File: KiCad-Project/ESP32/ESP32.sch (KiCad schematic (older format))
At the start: 14 parts, among them J3 UART, SW1 RESET, U3 AMS1117-3.3, U4 ESP32-WROOM-32

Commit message: swap out 603 resistors for 805
Give us more room to work with if we have to fix something.
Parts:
- R10: footprint Resistor_SMD:R_0201_0603Metric -> Resistor_SMD:R_0805_2012Metric; JLCPCB_PNUM C8218 -> C17540; MFG_PNUM 0603WAF2000T5E -> 0805W8F2000T5E; PACKAGE 0603 -> 0805
- R8: footprint Resistor_SMD:R_0201_0603Metric -> Resistor_SMD:R_0805_2012Metric; JLCPCB_PNUM C21190 -> C17513; MFG_PNUM 0603WAF1001T5E -> 0805W8F1001T5E; PACKAGE 0603 -> 0805
- R9: footprint Resistor_SMD:R_0201_0603Metric -> Resistor_SMD:R_0805_2012Metric; JLCPCB_PNUM C25804 -> C17414; MFG_PNUM 0603WAF1002T5E -> 0805W8F1002T5E; PACKAGE 0603 -> 0805
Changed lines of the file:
@@
 F 0 "R8" H 1609 1796 50  0000 L CNN
 F 1 "1K" H 1609 1705 50  0000 L CNN
-F 2 "Resistor_SMD:R_0201_0603Metric" H 1550 1750 50  0001 C CNN
+F 2 "Resistor_SMD:R_0805_2012Metric" H 1550 1750 50  0001 C CNN
 F 3 "~" H 1550 1750 50  0001 C CNN
-F 4 "C21190" H 1550 1750 50  0001 C CNN "JLCPCB_PNUM"
-F 5 "0603WAF1001T5E" H 1550 1750 50  0001 C CNN "MFG_PNUM"
-F 6 "0603" H 1550 1750 50  0001 C CNN "PACKAGE"
+F 4 "C17513" H 1550 1750 50  0001 C CNN "JLCPCB_PNUM"
+F 5 "0805W8F1001T5E" H 1550 1750 50  0001 C CNN "MFG_PNUM"
+F 6 "0805" H 1550 1750 50  0001 C CNN "PACKAGE"
 F 7 "JLCPCB" H 1550 1750 50  0001 C CNN "SUPPLIER"
 	1    1550 1750
@@
 F 0 "R9" H 2359 3596 50  0000 L CNN
 F 1 "10K" H 2359 3505 50  0000 L CNN
-F 2 "Resistor_SMD:R_0201_0603Metric" H 2300 3550 50  0001 C CNN
+F 2 "Resistor_SMD:R_0805_2012Metric" H 2300 3550 50  0001 C CNN
 F 3 "~" H 2300 3550 50  0001 C CNN
-F 4 "C25804" H 2300 3550 50  0001 C CNN "JLCPCB_PNUM"
-F 5 "0603WAF1002T5E" H 2300 3550 50  0001 C CNN "MFG_PNUM"
-F 6 "0603" H 2300 3550 50  0001 C CNN "PACKAGE"
+F 4 "C17414" H 2300 3550 50  0001 C CNN "JLCPCB_PNUM"
+F 5 "0805W8F1002T5E" H 2300 3550 50  0001 C CNN "MFG_PNUM"
+F 6 "0805" H 2300 3550 50  0001 C CNN "PACKAGE"
 F 7 "JLCPCB" H 2300 3550 50  0001 C CNN "SUPPLIER"
 	1    2300 3550
@@
 F 0 "R10" V 9050 2500 50  0000 L CNN
 F 1 "200" V 9250 2500 50  0000 L CNN
-F 2 "Resistor_SMD:R_0201_0603Metric" H 9150 2550 50  0001 C CNN
+F 2 "Resistor_SMD:R_0805_2012Metric" H 9150 2550 50  0001 C CNN
 F 3 "~" H 9150 2550 50  0001 C CNN
-F 4 "C8218" H 9150 2550 50  0001 C CNN "JLCPCB_PNUM"
-F 5 "0603WAF2000T5E" H 9150 2550 50  0001 C CNN "MFG_PNUM"
-F 6 "0603" H 9150 2550 50  0001 C CNN "PACKAGE"
+F 4 "C17540" H 9150 2550 50  0001 C CNN "JLCPCB_PNUM"
+F 5 "0805W8F2000T5E" H 9150 2550 50  0001 C CNN "MFG_PNUM"
+F 6 "0805" H 9150 2550 50  0001 C CNN "PACKAGE"
 F 7 "JLCPCB" H 9150 2550 50  0001 C CNN "SUPPLIER"
 	1    9150 2550

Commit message: Fixes in prep for printing
Making sure tolerance are in-spec for JLC PCB
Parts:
- U4: JLCPCB_PNUM (none) -> C82899; MFG_PNUM (none) -> ESP32-WROOM-32; PACKAGE (none) -> QFN-38_EP_18.0x25.0x1.27P; SUPPLIER (none) -> JLCPCB
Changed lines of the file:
@@
 F 2 "RF_Module:ESP32-WROOM-32" H 7750 1550 50  0001 C CNN
 F 3 "https://www.espressif.com/sites/default/files/documentation/esp32-wroom-32_datasheet_en.pdf" H 7450 3100 50  0001 C CNN
+F 4 "C82899" H 7750 3050 50  0001 C CNN "JLCPCB_PNUM"
+F 5 "ESP32-WROOM-32" H 7750 3050 50  0001 C CNN "MFG_PNUM"
+F 6 "QFN-38_EP_18.0x25.0x1.27P" H 7750 3050 50  0001 C CNN "PACKAGE"
+F 7 "JLCPCB" H 7750 3050 50  0001 C CNN "SUPPLIER"
 	1    7750 3050
 	1    0    0    -1

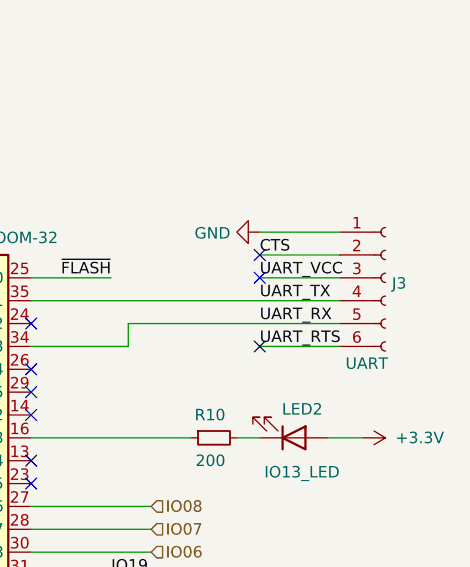
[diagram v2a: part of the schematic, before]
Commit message: Fix pin header
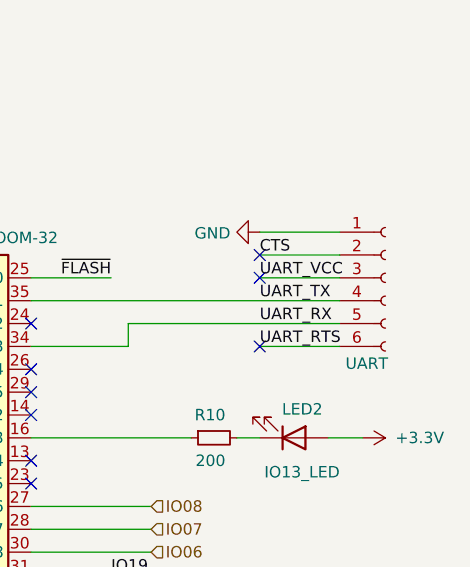
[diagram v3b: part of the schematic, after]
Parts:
- J3: footprint Connector_PinHeader_1.27mm:PinHeader_1x06_P1.27mm_Vertical -> Connector_PinSocket_2.54mm:PinSocket_1x06_P2.54mm_Vertical
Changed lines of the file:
@@
 U 1 1 61877E1E
 P 9900 1850
-F 0 "J3" H 9928 1826 50  0000 L CNN
+F 0 "J3" H 9928 1826 50  0001 L CNN
 F 1 "UART" H 9725 1475 50  0000 L CNN
-F 2 "Connector_PinHeader_1.27mm:PinHeader_1x06_P1.27mm_Vertical" H 9900 1850 50  0001 C CNN
+F 2 "Connector_PinSocket_2.54mm:PinSocket_1x06_P2.54mm_Vertical" H 9900 1850 50  0001 C CNN
 F 3 "~" H 9900 1850 50  0001 C CNN
 F 4 "Mouser" H 9900 1850 50  0001 C CNN "SUPPLIER"

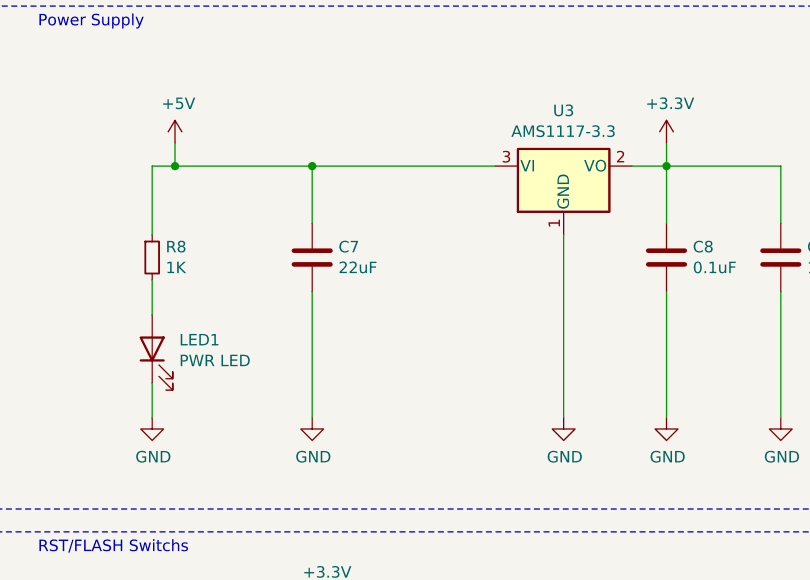
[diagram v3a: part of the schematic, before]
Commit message: Removed reverse voltage and increased size of power traces
Reverse voltage needed different components for 24 volt, and was a nice to have, so to keep cost down, opted to remove it.
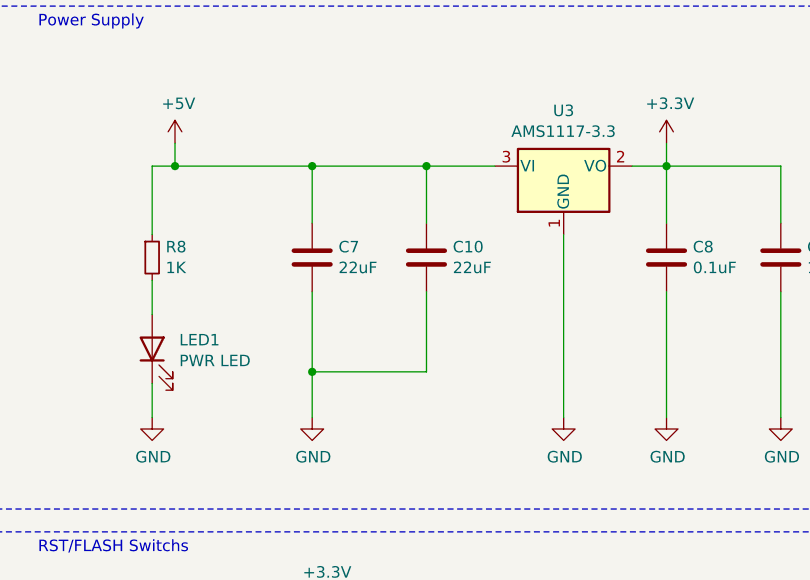
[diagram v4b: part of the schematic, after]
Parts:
- added C10: 22uF, Capacitor_SMD:C_0805_2012Metric, symbol Device:C
- JP1: footprint Connector_PinHeader_1.27mm:PinHeader_1x02_P1.27mm_Vertical -> Connector_PinHeader_2.54mm:PinHeader_1x02_P2.54mm_Vertical
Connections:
- net +5V: now also C10.1
- net GND: now also C10.2
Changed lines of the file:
@@
 $EndComp
 Wire Wire Line
-	3050 1350 2250 1350
+	3050 1350 2750 1350
 Wire Wire Line
 	1550 1350 1550 1650
@@
 $EndComp
 Wire Wire Line
-	2250 1900 2250 2450
+	2250 1900 2250 2250
 $Comp
 L power:GND #PWR018
@@
 Wire Wire Line
 	3100 4100 3100 3950
-Wire Wire Line
-	3100 3950 3450 3950
 Text Label 2850 3850 2    50   ~ 0
 ~RESET
@@
 UART_VCC
 NoConn ~ 9350 1850
-$Comp
-L Device:Jumper_NO_Small JP1
-U 1 1 6189F27D
-P 3550 3950
-F 0 "JP1" H 3550 4135 50  0000 C CNN
-F 1 "FLASH" H 3550 4044 50  0000 C CNN
-F 2 "Connector_PinHeader_1.27mm:PinHeader_1x02_P1.27mm_Vertical" H 3550 3950 50  0001 C CNN
-F 3 "~" H 3550 3950 50  0001 C CNN
-F 4 "Mouser" H 3550 3950 50  0001 C CNN "SUPPLIER"
-	1    3550 3950
-	1    0    0    -1
-$EndComp
-Wire Wire Line
-	3650 3950 4700 3950
 Wire Wire Line
 	8775 2050 8775 2150
@@
 Wire Wire Line
 	8350 2550 9050 2550
+Wire Wire Line
+	3650 3950 4700 3950
+Wire Wire Line
+	3100 3950 3450 3950
+$Comp
+L Device:Jumper_NO_Small JP1
+U 1 1 6189F27D
+P 3550 3950
+F 0 "JP1" H 3550 4135 50  0000 C CNN
+F 1 "FLASH" H 3550 4044 50  0000 C CNN
+F 2 "Connector_PinHeader_2.54mm:PinHeader_1x02_P2.54mm_Vertical" H 3550 3950 50  0001 C CNN
+F 3 "~" H 3550 3950 50  0001 C CNN
+F 4 "Mouser" H 3550 3950 50  0001 C CNN "SUPPLIER"
+	1    3550 3950
+	1    0    0    -1
+$EndComp
+$Comp
+L Device:C C10
+U 1 1 61B24BD4
+P 2750 1750
+F 0 "C10" H 2865 1796 50  0000 L CNN
+F 1 "22uF" H 2865 1705 50  0000 L CNN
+F 2 "Capacitor_SMD:C_0805_2012Metric" H 2788 1600 50  0001 C CNN
+F 3 "~" H 2750 1750 50  0001 C CNN
+F 4 "C45783" H 2750 1750 50  0001 C CNN "JLCPCB_PNUM"
+F 5 "CL21A226MAQNNNE" H 2750 1750 50  0001 C CNN "MFG_PNUM"
+F 6 "0805" H 2750 1750 50  0001 C CNN "PACKAGE"
+F 7 "JLCPCB" H 2750 1750 50  0001 C CNN "SUPPLIER"
+	1    2750 1750
+	1    0    0    -1
+$EndComp
+Wire Wire Line
+	2750 1600 2750 1350
+Connection ~ 2750 1350
+Wire Wire Line
+	2750 1350 2250 1350
+Wire Wire Line
+	2750 1900 2750 2250
+Wire Wire Line
+	2750 2250 2250 2250
+Connection ~ 2250 2250
+Wire Wire Line
+	2250 2250 2250 2450
 $EndSCHEMATC

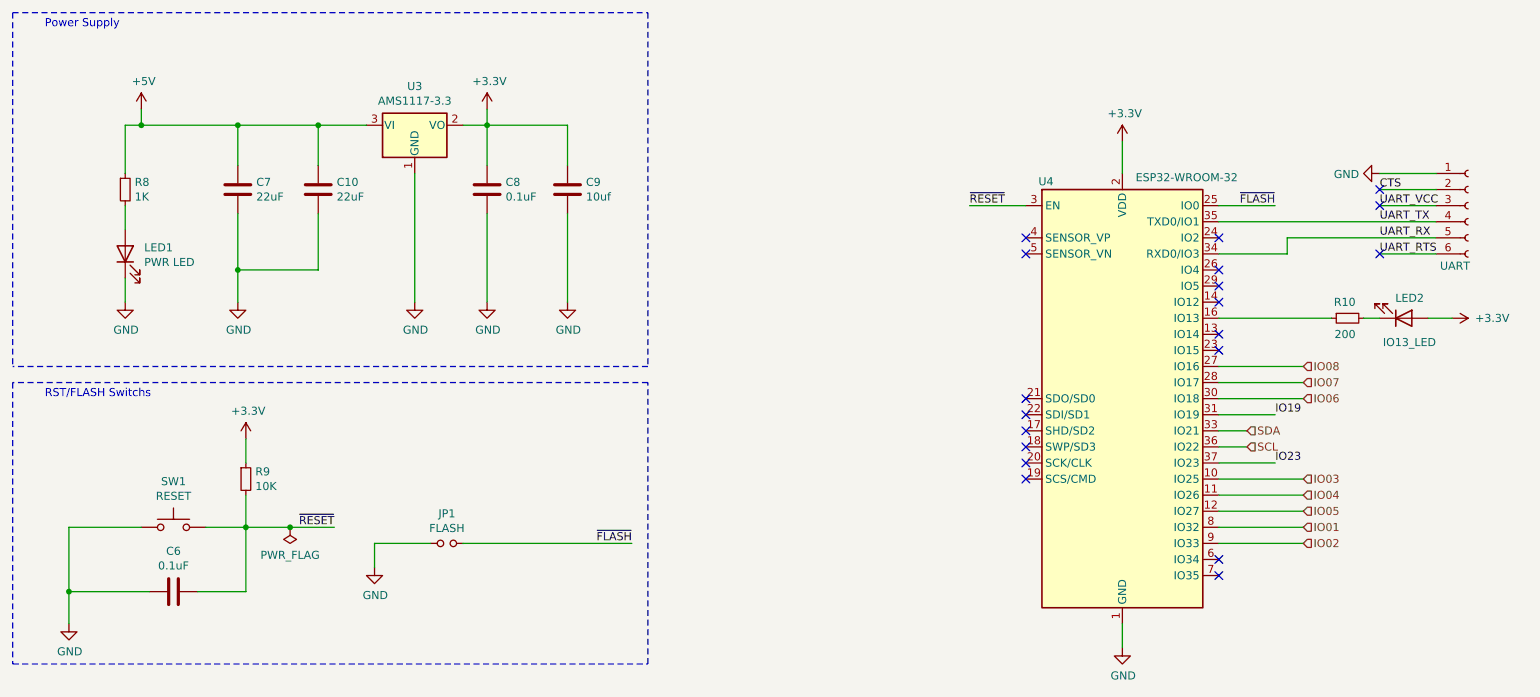
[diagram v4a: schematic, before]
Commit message: Jumper to connect UART VCC to 5v
Allow powering the 3v-5v side from the UART conector.
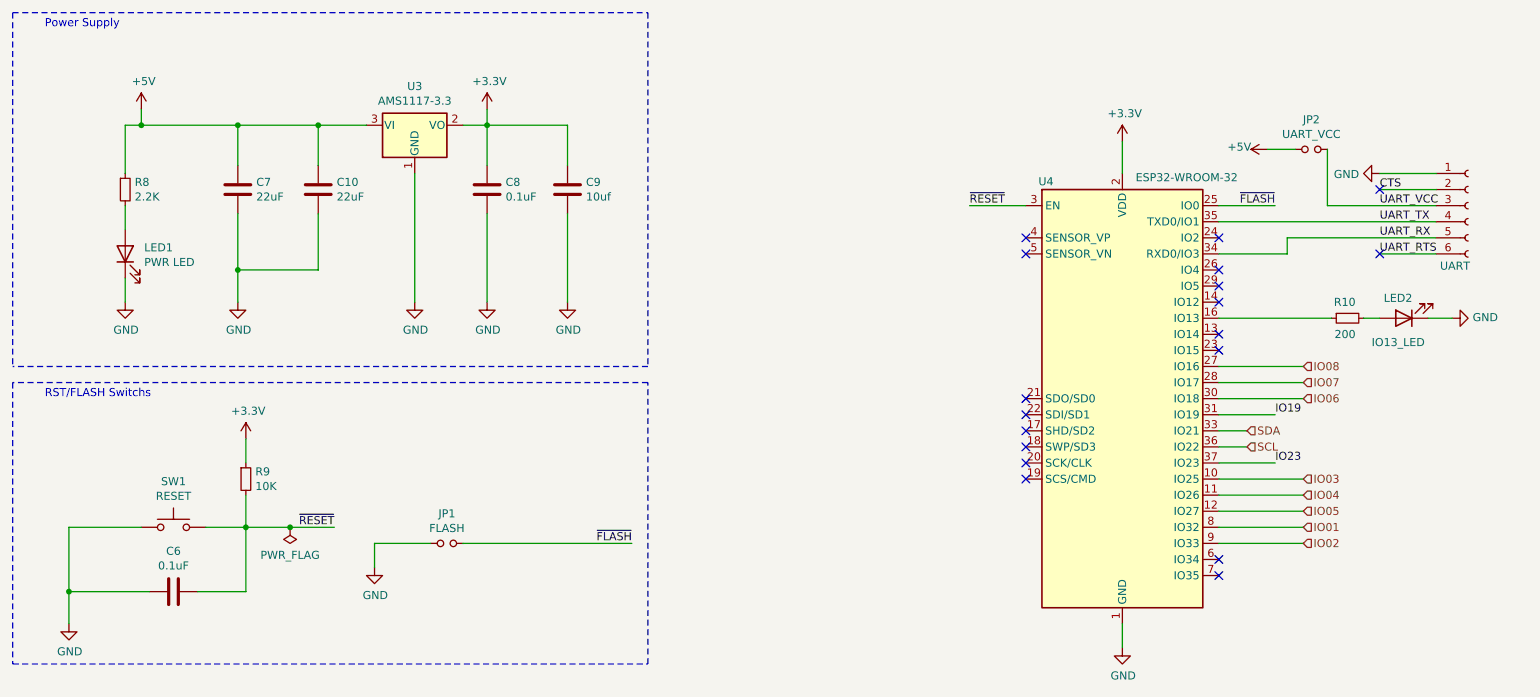
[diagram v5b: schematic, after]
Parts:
- added JP2: UART_VCC, Connector_PinHeader_2.54mm:PinHeader_1x02_P2.54mm_Vertical, symbol Device:Jumper_NO_Small
- R8: value 1K -> 2.2K; JLCPCB_PNUM C17513 -> C17520; MFG_PNUM 0805W8F1001T5E -> 0805W8F2201T5E
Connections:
- net +3V3: no longer LED2.2 (A)
- net +5V: now also JP2.1
- net GND: now also LED2.1 (K)
- net UART_VCC: now also JP2.2
- net at R10.2: now also LED2.2 (A); no longer LED2.1 (K)
- no-connect marks 19 -> 18
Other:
- moved on the sheet: LED2
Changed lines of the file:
@@
 P 1550 1750
 F 0 "R8" H 1609 1796 50  0000 L CNN
-F 1 "1K" H 1609 1705 50  0000 L CNN
+F 1 "2.2K" H 1609 1705 50  0000 L CNN
 F 2 "Resistor_SMD:R_0805_2012Metric" H 1550 1750 50  0001 C CNN
 F 3 "~" H 1550 1750 50  0001 C CNN
-F 4 "C17513" H 1550 1750 50  0001 C CNN "JLCPCB_PNUM"
-F 5 "0805W8F1001T5E" H 1550 1750 50  0001 C CNN "MFG_PNUM"
+F 4 "C17520" H 1550 1750 50  0001 C CNN "JLCPCB_PNUM"
+F 5 "0805W8F2201T5E" H 1550 1750 50  0001 C CNN "MFG_PNUM"
 F 6 "0805" H 1550 1750 50  0001 C CNN "PACKAGE"
 F 7 "JLCPCB" H 1550 1750 50  0001 C CNN "SUPPLIER"
@@
 	9700 2150 9350 2150
 Wire Wire Line
-	9700 1850 9350 1850
-Wire Wire Line
 	9700 1750 9350 1750
 Wire Wire Line
@@
 F 7 "JLCPCB" H 9500 2550 50  0001 C CNN "SUPPLIER"
 	1    9500 2550
-	1    0    0    1
+	-1   0    0    1
 $EndComp
 $Comp
@@
 Wire Wire Line
 	9350 2550 9250 2550
-$Comp
-L power:+3.3V #PWR022
-U 1 1 618A9CE7
-P 9800 2550
-F 0 "#PWR022" H 9800 2400 50  0001 C CNN
-F 1 "+3.3V" V 9800 2800 50  0000 C CNN
-F 2 "" H 9800 2550 50  0001 C CNN
-F 3 "" H 9800 2550 50  0001 C CNN
-	1    9800 2550
-	0    1    -1   0
-$EndComp
 Wire Wire Line
 	9800 2550 9650 2550
@@
 Text Label 9350 1850 0    50   ~ 0
 UART_VCC
-NoConn ~ 9350 1850
 Wire Wire Line
 	8775 2050 8775 2150
@@
 Wire Wire Line
 	2250 2250 2250 2450
+$Comp
+L power:+5V #PWR023
+U 1 1 61B4BBED
+P 8650 1500
+F 0 "#PWR023" H 8650 1350 50  0001 C CNN
+F 1 "+5V" V 8665 1673 50  0000 C CNN
+F 2 "" H 8650 1500 50  0001 C CNN
+F 3 "" H 8650 1500 50  0001 C CNN
+	1    8650 1500
+	0    -1   -1   0
+$EndComp
+$Comp
+L Device:Jumper_NO_Small JP2
+U 1 1 61B4F51D
+P 8925 1500
+F 0 "JP2" H 8925 1685 50  0000 C CNN
+F 1 "UART_VCC" H 8925 1594 50  0000 C CNN
+F 2 "Connector_PinHeader_2.54mm:PinHeader_1x02_P2.54mm_Vertical" H 8925 1500 50  0001 C CNN
+F 3 "~" H 8925 1500 50  0001 C CNN
+F 4 "Mouser" H 8925 1500 50  0001 C CNN "SUPPLIER"
+	1    8925 1500
+	1    0    0    -1
+$EndComp
+Wire Wire Line
+	9025 1500 9025 1850
+Wire Wire Line
+	9025 1850 9700 1850
+Wire Wire Line
+	8650 1500 8825 1500
+$Comp
+L power:GND #PWR?
+U 1 1 61B80328
+P 9800 2550
+F 0 "#PWR?" H 9800 2300 50  0001 C CNN
+F 1 "GND" V 9805 2422 50  0000 R CNN
+F 2 "" H 9800 2550 50  0001 C CNN
+F 3 "" H 9800 2550 50  0001 C CNN
+	1    9800 2550
+	0    -1   -1   0
+$EndComp
 $EndSCHEMATC

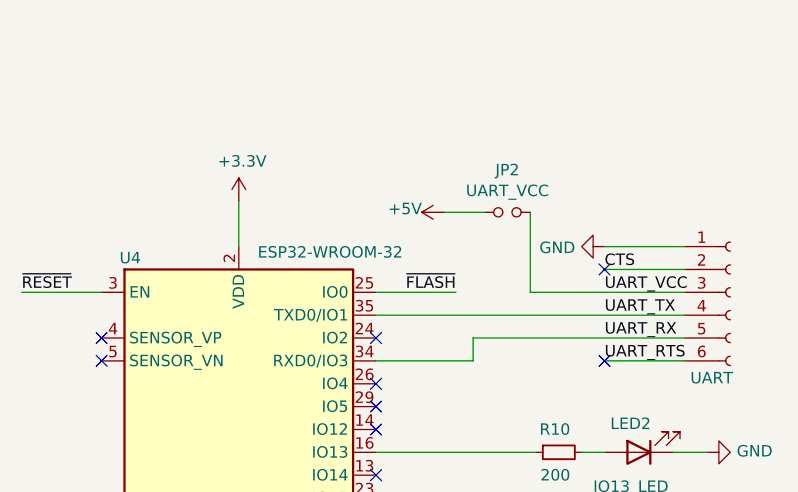
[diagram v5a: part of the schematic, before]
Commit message: Update fill zones
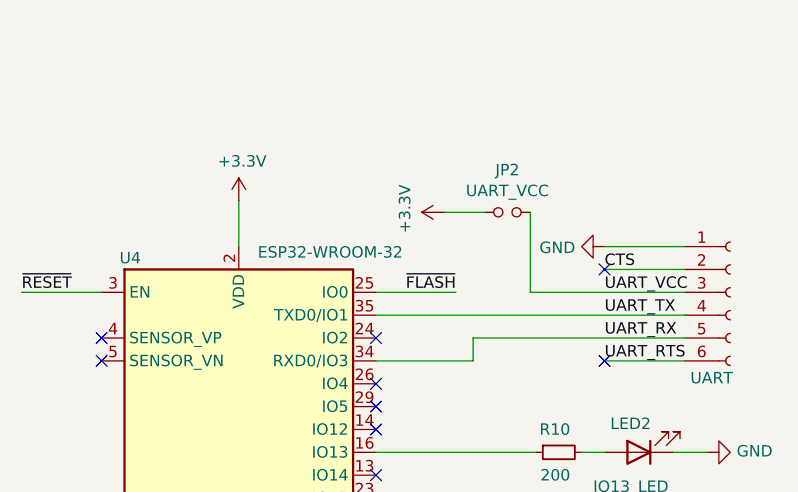
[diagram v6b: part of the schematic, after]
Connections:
- net +3V3: now also JP2.1
- net +5V: no longer JP2.1
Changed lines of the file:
@@
 	2250 2250 2250 2450
-$Comp
-L power:+5V #PWR023
-U 1 1 61B4BBED
-P 8650 1500
-F 0 "#PWR023" H 8650 1350 50  0001 C CNN
-F 1 "+5V" V 8665 1673 50  0000 C CNN
-F 2 "" H 8650 1500 50  0001 C CNN
-F 3 "" H 8650 1500 50  0001 C CNN
-	1    8650 1500
-	0    -1   -1   0
-$EndComp
 $Comp
 L Device:Jumper_NO_Small JP2
@@
 	0    -1   -1   0
 $EndComp
+$Comp
+L power:+3.3V #PWR?
+U 1 1 61A96D0C
+P 8650 1500
+F 0 "#PWR?" H 8650 1350 50  0001 C CNN
+F 1 "+3.3V" H 8665 1673 50  0000 C CNN
+F 2 "" H 8650 1500 50  0001 C CNN
+F 3 "" H 8650 1500 50  0001 C CNN
+	1    8650 1500
+	0    -1   -1   0
+$EndComp
